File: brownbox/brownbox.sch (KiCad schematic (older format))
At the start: 340 parts, among them J1 Rifle Connector - C7-205, J2 12-Pin Cinch Jones Expansion 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

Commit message: All parts placed, values verified
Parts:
- removed C?: 0.1uF, symbol Device:C
- removed C?: 100pF, symbol Device:C
- removed R?: 15K, symbol Device:R_US
- added C?: 9-35pF, symbol Device:CTRIM_Small
- added R?: 100K, symbol Device:R_US
- added SW? (x2): SW_Push_3PDT, symbol Switch:SW_Push_3PDT
- C?: value 0.22uF -> 0.3uF
- C? (x3): value 100pF -> 0.01uF
- C? (x2): value 100pF -> 0.1uF
- C?: value 100pF -> 180pF
- C?: value 100pF -> 82pF
- C?: value 750pF -> 56pF
- C?: value 750pF -> 180pF
- C?: value 100pF -> 120pF
- C?: value 62pF -> 360pF
- C?: value 100pF -> 27pF
- C? (x2): value 100uF -> 10uF
- L?: value L -> 4 Turns, #16 brass
- R? (x3): value 2K -> 5.1K
- R? (x3): value 2K -> 51K
- R? (x2): value 10K -> 5.1K
- R? (x2): value 2K -> 10K
- R?: value 10K -> 12K
- R? (x4): value 10K -> 1K
- R?: value 10K -> 2K
- R?: value 1K -> 100K
- R?: value 10K -> 51K
- R?: value 2K -> 33K
- R?: value 510K -> 100K
- R?: value 2K -> 22K
- R? (x6): value 22K -> 100K
- R? (x2): value 10K -> 100K
- R? (x4): value 22K -> 10K
- R?: value 22K -> 2K
- R?: value 22K -> 12K
- R?: value 10K -> 1.8K
- R? (x2): value 10K -> 150K
- R? (x4): value 22K -> 5.1K
- R?: value 10K -> 300K
- R?: value 10K -> 6.2K
- R?: value 22K -> 6.2K
- R?: value 10K -> 15K
- R?: value 22K -> 51K
- R? (x2): value 10K -> 22K
- R? (x2): value 10K -> 100
- RV? (x2): value 10K -> 5K
- T?: value Transformer_1P_SS -> CF104 core, #22 wire
- X?: value Crystal_Small -> 3.579545Mhz
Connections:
- net E: now also SW?.7
- net E': now also SW?.3
- net F: now also SW?.7
- net F': now also SW?.3
- net GNDREF: now also C?.2, C?.2, R?.2, R?.2, C?.2, SW?.4, SW?.4, SW?.6, SW?.6, SW?.8, SW?.8
- net S4A3: now also R?.1, R?.1, R?.2
- net at Q?.2 (B): now also Q?.3 (C), R?.2
- net at Q?.3 (C), R?.2, R?.2: now also R?.1; no longer Q?.2 (B), R?.2
- net at C?.1, L?.2: now also C?.1
- net at D?.2 (A), R?.2: now also SW?.5 (x2)
- net at R?.2: now also SW?.9
- net at R?.1: now also SW?.9
- net at R?.1: now also SW?.11
- net at R?.2: now also SW?.11
- net at C?.1: now also SW?.10, SW?.12 (x2)
- new net: Q?.2 (B), R?.2, R?.2
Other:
- note added: "2 turns"
- note added: "22 turns"
- moved on the sheet: BT?, C?, J1, J2, R?

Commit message: Update RefDes's
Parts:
- C41: renamed from C?; value 0.1uF -> 0.01uF
- R134, R135: renamed from R?; value 22K -> 10K
- R88: renamed from R?; value 22K -> 270
- gave numbers to parts that had none: 306
- renumbered R3 to R2, R4 to R3, R6 to R4, R2 to R5, R5 to R6

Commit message: A few more Refdes's
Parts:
- gave numbers to parts that had none: 4
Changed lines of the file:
@@
 	3850 13100 3950 13100
 $Comp
-L Device:Jumper JP?
+L Device:Jumper J3
 U 1 1 67B9B341
 P 3450 12400
-F 0 "JP?" V 3404 12527 50  0000 L CNN
+F 0 "J3" V 3404 12527 50  0000 L CNN
 F 1 "Jumper" V 3495 12527 50  0000 L CNN
 F 2 "" H 3450 12400 50  0001 C CNN
@@
 Connection ~ 7750 15300
 $Comp
-L Device:L L?
-U 1 1 6AAAC7F4
-P 7250 15600
-F 0 "L?" H 7206 15554 50  0000 R CNN
-F 1 "L" H 7206 15645 50  0000 R CNN
-F 2 "" H 7250 15600 50  0001 C CNN
-F 3 "~" H 7250 15600 50  0001 C CNN
-	1    7250 15600
-	-1   0    0    1
-$EndComp
-$Comp
 L Device:R_US R88
 U 1 1 6AAAF573
@@
 	9600 15850 9800 15850
 $Comp
-L Device:Battery_Cell BT?
+L Device:Battery_Cell BT1
 U 1 1 77F9C5A7
 P 10500 15850
-F 0 "BT?" V 10755 15900 50  0000 C CNN
+F 0 "BT1" V 10755 15900 50  0000 C CNN
 F 1 "4 D Cells" V 10664 15900 50  0000 C CNN
 F 2 "" V 10500 15910 50  0001 C CNN
@@
 	19950 9400 20500 9400
 $Comp
-L Device:Battery_Cell BT?
+L Device:Battery_Cell BT2
 U 1 1 7A1112B4
 P 20950 9650
-F 0 "BT?" H 21200 9800 50  0000 C CNN
+F 0 "BT2" H 21200 9800 50  0000 C CNN
 F 1 "1 C Cell" H 21250 9700 50  0000 C CNN
 F 2 "" V 20950 9710 50  0001 C CNN
@@
 	0    -1   -1   0
 $EndComp
+$Comp
+L Device:L L2
+U 1 1 6AAAC7F4
+P 7250 15600
+F 0 "L2" H 7206 15554 50  0000 R CNN
+F 1 "L" H 7206 15645 50  0000 R CNN
+F 2 "" H 7250 15600 50  0001 C CNN
+F 3 "~" H 7250 15600 50  0001 C CNN
+	1    7250 15600
+	-1   0    0    1
+$EndComp
 $EndSCHEMATC

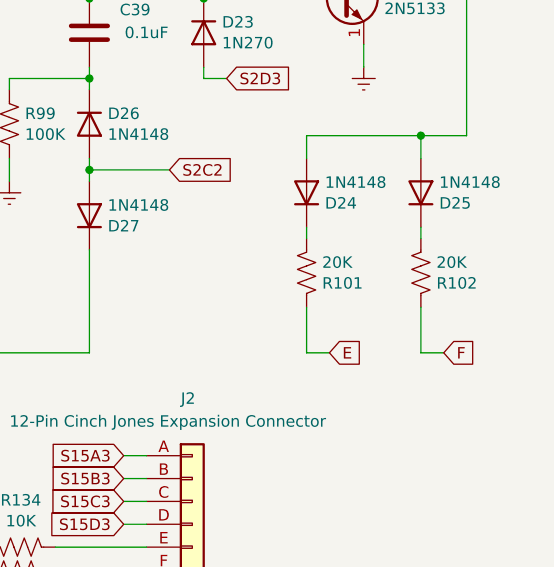
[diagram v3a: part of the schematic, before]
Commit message: Fix duplicate Refdes - annotation complete
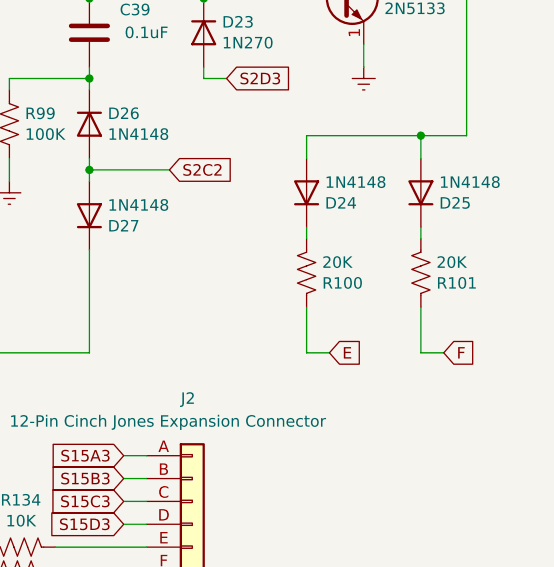
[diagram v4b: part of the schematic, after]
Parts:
- renumbered R101 to R100, R102 to R101
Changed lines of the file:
@@
 	20000 5900 20100 5900
 $Comp
-L Device:R_US R101
+L Device:R_US R100
 U 1 1 63F6AA1A
 P 20450 6750
-F 0 "R101" H 20518 6796 50  0000 L CNN
+F 0 "R100" H 20518 6796 50  0000 L CNN
 F 1 "20K" H 20518 6705 50  0000 L CNN
 F 2 "" V 20490 6740 50  0001 C CNN
@@
 	20450 6600 20450 6550
 $Comp
-L Device:R_US R102
+L Device:R_US R101
 U 1 1 64034339
 P 20950 6750
-F 0 "R102" H 21018 6796 50  0000 L CNN
+F 0 "R101" H 21018 6796 50  0000 L CNN
 F 1 "20K" H 21018 6705 50  0000 L CNN
 F 2 "" V 20990 6740 50  0001 C CNN
